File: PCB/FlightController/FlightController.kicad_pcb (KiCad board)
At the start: 2 copper layers, 101.6 x 101.6 mm, 13 parts, among them J2 +, J3 -, J4 BATT Reg IC, J5 Feedback This Side, J6 Connect The Hall Circuit Here!, U1 nRF52840 (Sense) WAS HERE, U2 RFM95W

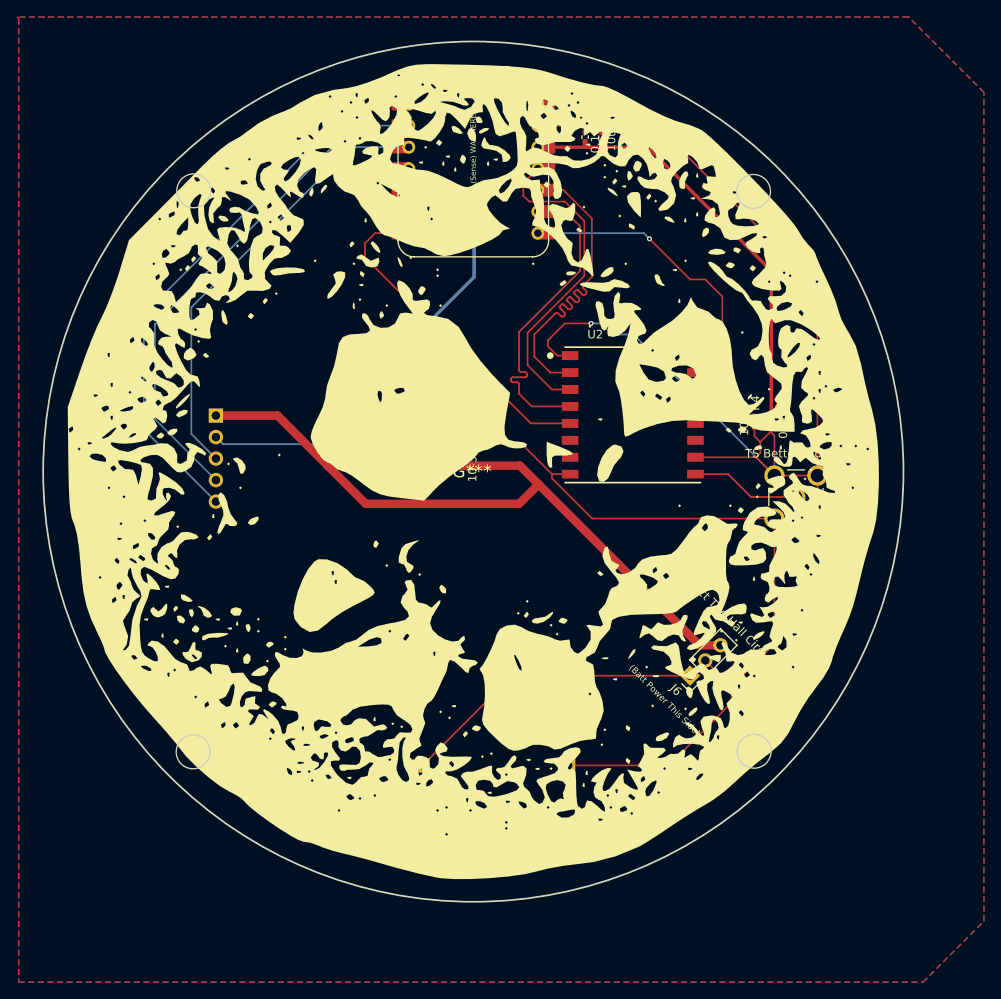
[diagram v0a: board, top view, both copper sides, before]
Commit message: added a P-mosfet for the 3.3v wiring and let the 3.3v regulator "pre-power" the (now 4) pin switch system for the hall effect magnet sensor.
added a P-mosfet for the 3.3v wiring and let the 3.3v regulator "pre-power" the (now 4) pin switch system for the hall effect magnet sensor.
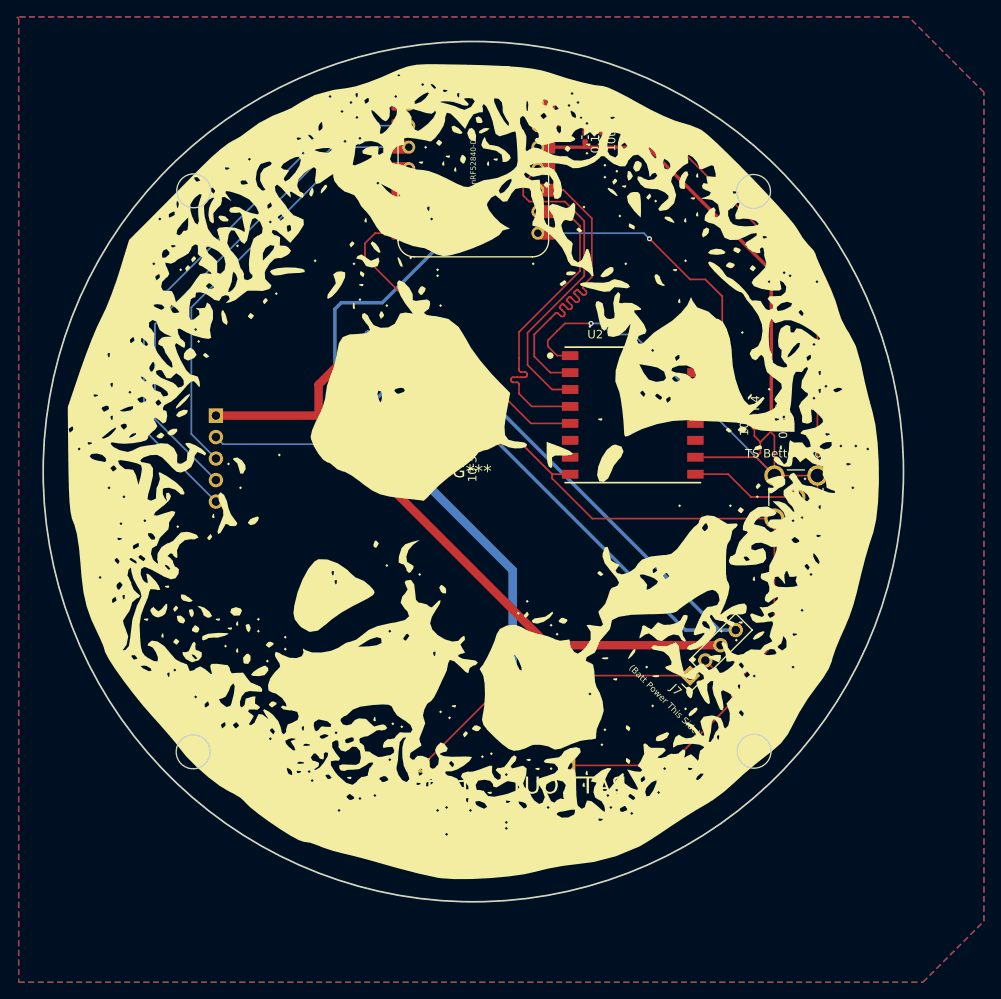
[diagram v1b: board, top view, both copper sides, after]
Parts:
- removed J6: Connect The Hall Circuit Here!, Connector_PinHeader_2.54mm:PinHeader_1x03_P2.54mm_Vertical
- added J7: HallCircuit, Connector_PinHeader_2.54mm:PinHeader_1x04_P2.54mm_Vertical, F.Cu at (166.7, 113.8)
- added Q1: P_CHANNEL, DMP3099L_7:DMP3099L-7_DIO, B.Cu at (132.5, 77.2)
- J2: value + -> BATT IN
- J3: value - -> BATT OUT
- J5: value Feedback This Side -> Pump
- U1: value nRF52840 (Sense) WAS HERE -> XIAO-nRF52840-DIP
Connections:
- J4 pad 3: RAWSWPOWER -> MAIN
- U1 pad 12: VOUT -> SWVOUT
- U2 pad 13: VOUT -> SWVOUT
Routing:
- net VOUT: track 100.3 -> 165.2 mm
- net SWVOUT: track 0.00 -> 51.6 mm
- net MAIN: track 36.0 -> 65.9 mm
- net RAWSWPOWER: track 98.5 -> 88.7 mm, vias 0 -> 1

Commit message: All boards should be finished. ACC otw, and an earlier version of the main board otw
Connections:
- Q1 pad 2: SWVOUT -> RAWSWPOWER
- Q1 pad 3: RAWSWPOWER -> SWVOUT
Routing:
- net SWVOUT: track 51.6 -> 31.6 mm
- net RAWSWPOWER: track 88.7 -> 83.0 mm
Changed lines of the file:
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@@
 			(size 0.8636 1.6002)
 			(layers "B.Cu" "B.Mask" "B.Paste")
-			(net 24 "SWVOUT")
+			(net 23 "RAWSWPOWER")
 			(pinfunction "2")
 			(pintype "unspecified")
@@
 			(size 0.8636 1.6002)
 			(layers "B.Cu" "B.Mask" "B.Paste")
-			(net 23 "RAWSWPOWER")
+			(net 24 "SWVOUT")
 			(pinfunction "3")
 			(pintype "unspecified")
@@
 	)
 	(segment
-		(start 122.83 79.42)
-		(end 122.83 83.08)
-		(width 1)
-		(layer "F.Cu")
-		(net 23)
-	)
-	(segment
 		(start 170.296051 110.203949)
 		(end 149.953949 110.203949)
@@
 	)
 	(segment
-		(start 127.75 74.5)
-		(end 122.83 79.42)
+		(start 129.1 83.1)
+		(end 129.08 83.08)
 		(width 1)
 		(layer "F.Cu")
 		(net 23)
 	)
+	(segment
+		(start 129.08 83.08)
+		(end 122.83 83.08)
+		(width 1)
+		(layer "F.Cu")
+		(net 23)
+	)
 	(via
-		(at 127.75 74.5)
+		(at 129.1 83.1)
 		(size 0.6)
 		(drill 0.3)
@@
 	)
 	(segment
-		(start 128.75 73.5)
-		(end 127.875 74.375)
+		(start 131.5 78.25)
+		(end 131.5 80.7)
 		(width 1)
 		(layer "B.Cu")
@@
 	)
 	(segment
-		(start 131.5 73.5)
-		(end 128.75 73.5)
+		(start 131.5 80.7)
+		(end 129.1 83.1)
 		(width 1)
 		(layer "B.Cu")
@@
 	)
 	(segment
-		(start 127.875 74.375)
-		(end 127.75 74.5)
-		(width 1)
-		(layer "B.Cu")
-		(net 23)
-	)
-	(segment
 		(start 132.450001 76.239)
-		(end 132.450001 74.450001)
-		(width 1)
-		(layer "B.Cu")
-		(net 23)
-	)
-	(segment
-		(start 132.450001 74.450001)
-		(end 131.5 73.5)
-		(width 1)
-		(layer "B.Cu")
-		(net 23)
-	)
-	(segment
-		(start 125.5 69.75)
-		(end 130.35 69.75)
-		(width 0.4)
+		(end 132.450001 67.649999)
+		(width 0.5)
 		(layer "B.Cu")
 		(net 24)
 	)
 	(segment
-		(start 124.75 70.5)
-		(end 125.5 69.75)
-		(width 0.4)
+		(start 132.450001 67.649999)
+		(end 148.72 51.38)
+		(width 0.5)
 		(layer "B.Cu")
 		(net 24)
-	)
-	(segment
-		(start 129 81.75)
-		(end 125.25 81.75)
-		(width 0.4)
-		(layer "B.Cu")
-		(net 24)
-	)
-	(segment
-		(start 131.5 79.25)
-		(end 129 81.75)
-		(width 0.4)
-		(layer "B.Cu")
-		(net 24)
-	)
-	(segment
-		(start 131.5 78.25)
-		(end 131.5 79.25)
-		(width 0.4)
-		(layer "B.Cu")
-		(net 24)
-	)
-	(segment
-		(start 125.25 81.75)
-		(end 124.75 81.25)
-		(width 0.4)
-		(layer "B.Cu")
-		(net 24)
-	)
-	(segment
-		(start 130.35 69.75)
-		(end 148.72 51.38)
-		(width 0.4)
-		(layer "B.Cu")
-		(net 24)
-	)
-	(segment
-		(start 124.75 81.25)
-		(end 124.75 70.5)
-		(width 0.4)
-		(layer "B.Cu")
-		(net 24)

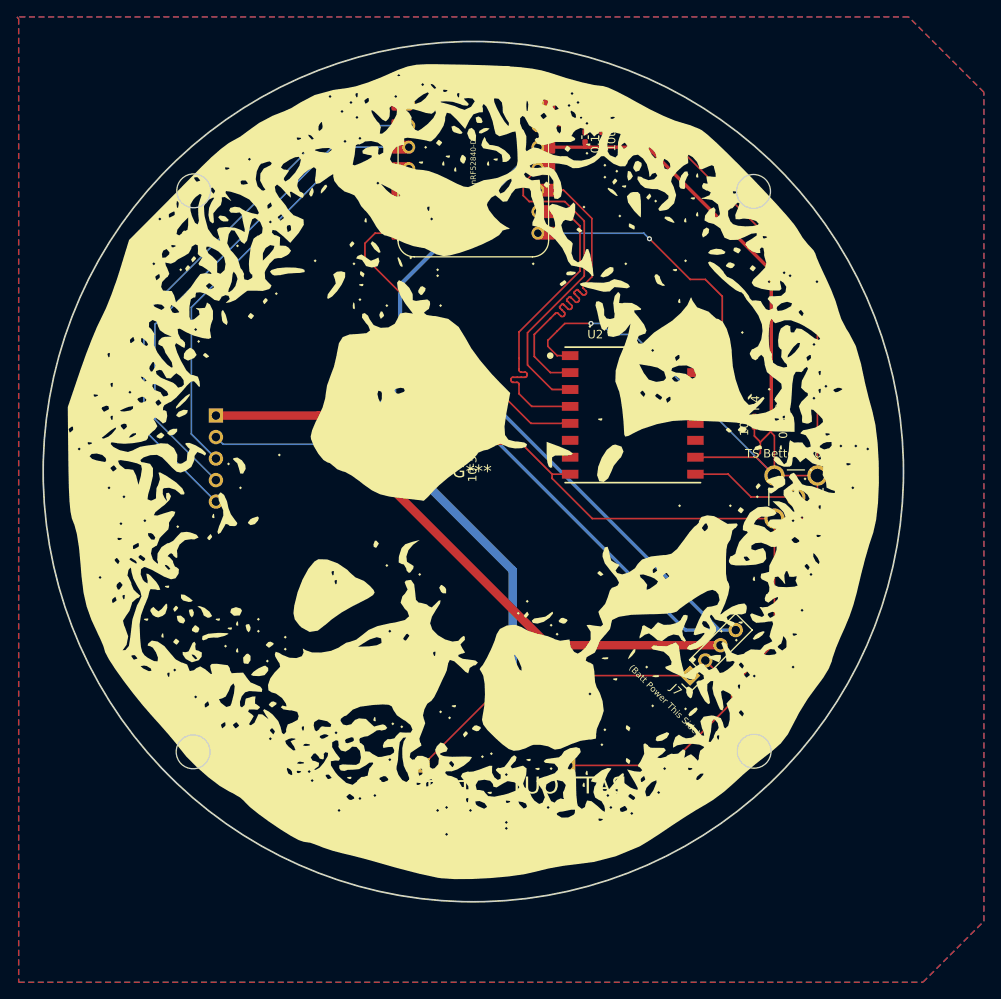
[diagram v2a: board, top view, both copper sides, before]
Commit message: post R1 - flipped many traces and worked on adding an internal sensor for reduncancy
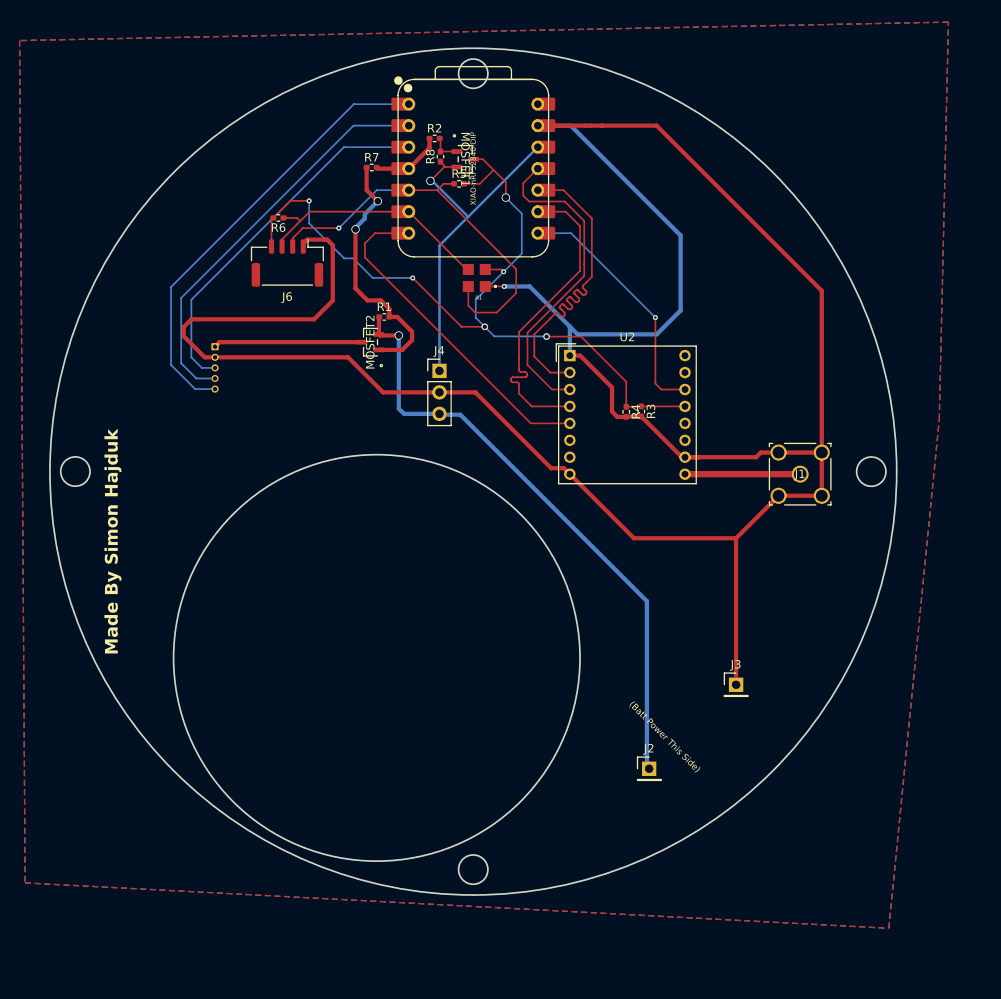
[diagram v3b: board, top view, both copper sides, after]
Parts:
- removed G***: LOGO, Cookie:GoodCooke
- removed J5: Pump, Connector_PinHeader_2.54mm:PinHeader_1x05_P2.54mm_Vertical
- removed J7: HallCircuit, Connector_PinHeader_2.54mm:PinHeader_1x04_P2.54mm_Vertical
- removed Q1: P_CHANNEL, DMP3099L_7:DMP3099L-7_DIO
- removed TS Better Work: SMA Connector, SMAFootprint:TE_5-1814832-2
- added A1: MS583702BA01-50, MS583702BA01_50:XDCR_MS583702BA01-50, F.Cu at (141.5, 66.8)
- added J1: SMA Connector, SMAv2:CONN_RF2-04A-T-00-50-G_ADM, F.Cu at (179.7, 90.0)
- added J6: Pressure sensor, Connector_JST:JST_GH_BM04B-GHS-TBT_1x04-1MP_P1.25mm_Vertical, F.Cu at (119.1, 65.1)
- added J8: 530470510, 530470510:MOLEX_530470510, B.Cu at (110.6, 75.0)
- added MOSFET1: DMP3068L-7, DMP3068L_7:SOT-23_DMP3068L_DIO, F.Cu at (140.1, 52.8)
- added MOSFET2: DMP3068L-7, DMP3068L_7:SOT-23_DMP3068L_DIO, F.Cu at (129.0, 74.4)
- added R5: 4.7k, Resistor_SMD:R_0402_1005Metric_Pad0.72x0.64mm_HandSolder, F.Cu at (139.4, 55.7)
- added R6: 4.7k, Resistor_SMD:R_0402_1005Metric_Pad0.72x0.64mm_HandSolder, F.Cu at (118.1, 59.7)
- added R7: 4.7k, Resistor_SMD:R_0402_1005Metric_Pad0.72x0.64mm_HandSolder, F.Cu at (129.1, 53.8)
- added R8: 10k, Resistor_SMD:R_0402_1005Metric_Pad0.72x0.64mm_HandSolder, F.Cu at (137.2, 52.5)
- J2, J3: moved to F.Cu
- R1: value 0.1uF -> 4.7k
- R2: value 10uF -> 4.7k
- U2: footprint RMF95W:XCVR_RFM95W-868S2 -> RF_Module:HOPERF_RFM9XW_THT
- moved R1 31.8 mm to (130.6, 71.4), turned to 0 degrees
- moved J2 26.8 mm to (161.9, 124.8), turned to 0 degrees
- moved J3 22.0 mm to (172.1, 114.9), turned to 0 degrees
- moved R2 19.8 mm to (136.5, 50.4), turned to 0 degrees
- moved R3 15.4 mm to (160.9, 82.6)
- moved R4 15.2 mm to (159.2, 82.6)
- moved U2 10.2 mm to (152.5, 76.0)
- moved J4 7.15 mm to (137.1, 77.8)
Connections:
- R1 pad 1: VOUT -> MAIN
- R1 pad 2: GND -> PWRSwitch
- R2 pad 1: VOUT -> PWRSwitch
- R2 pad 2: GND -> PWRSwitch
- R3 pad 1: VOUT -> SW3v3
- R4 pad 1: VOUT -> SW3v3
- U1 pad 12: SWVOUT -> VOUT
- U1 pad 4: unconnected-(U1-PA11_A3_D3-Pad4) -> PWRSwitch
- U1 pad 5: unconnected-(U1-PA8_A4_D4_SDA-Pad5) -> SDA
- U1 pad 6: unconnected-(U1-PA9_A5_D5_SCL-Pad6) -> SCL
- U2 pad 13: SWVOUT -> SW3v3
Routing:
- net VOUT: track 165.2 -> 42.1 mm, vias 0 -> 1
- net SW3v3: track 0.00 -> 98.5 mm, vias 0 -> 6
- net RAWSWPOWER: track 83.0 -> 17.6 mm, vias 1 -> 0
- net SDA: track 0.00 -> 47.9 mm, vias 0 -> 1
- net PWRSwitch: track 0.00 -> 42.6 mm, vias 0 -> 2
- net GND: track 264.9 -> 299.9 mm
- net SWVOUT: track 31.6 -> 0.00 mm
- net SCL: track 0.00 -> 29.2 mm
- net FEEDBACK: track 67.2 -> 52.6 mm
- net DIR: track 61.1 -> 47.8 mm
- net PWM: track 52.6 -> 43.3 mm
- net INT: track 38.3 -> 29.6 mm
- net MAIN: track 65.9 -> 71.4 mm, vias 0 -> 1
- net ANT: track 13.0 -> 13.6 mm
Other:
- board size 101.6 x 101.6 mm -> 100 x 100 mm
- board text added: "Made By Simon Hajduk"
- board text removed: "0.1uF"
- board text removed: "10-33 uF"
- board text removed: "10uF"
